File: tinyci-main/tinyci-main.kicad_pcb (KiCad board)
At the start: 2 copper layers, 110 x 82.5 mm, 56 parts, among them J1 Jack-DC, J2 Jack-DC, J3 Jack-DC, J4 Conn_01x13_Male, J5 Conn_01x13_Male, J6 Jack-DC, J7 Jack-DC, J8 Conn_01x04_Male, J9 Conn_01x04_Male, K1 SANYOU_SRD_Form_C, K2 SANYOU_SRD_Form_C, K3 SANYOU_SRD_Form_C, K4 SANYOU_SRD_Form_C, Q1 BC337, Q2 BC337, Q3 BC337, Q4 BC337, U1 AMS1117-3.3

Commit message: Version v0.5
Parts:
- removed G***: LOGO, tinyci:just-ci-it
- J8, J9: value Conn_01x04_Male -> Conn_01x06_Male
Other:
- board text added: "TinyCI v0.5"
- board text added: "TinyCI v0.5 http://github.com/superna9999/tinyci"
- board text removed: "TinyCI v0.4"
- board text removed: "TinyCI v0.4 http://github.com/superna9999/tinyci"

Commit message: fixup! Version v0.5
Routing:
- net VDC: track 136.6 -> 143.7 mm
- net /485_EN: track 55.4 -> 52.2 mm
- net /CFG: track 63.3 -> 60.2 mm
- net /IO17: track 40.7 -> 39.4 mm
- net /IO12: track 45.6 -> 44.5 mm
- net /IO5: track 48.1 -> 47.0 mm
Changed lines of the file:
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@@
     (thickness 1.6)
     (drawings 39)
-    (tracks 267)
+    (tracks 268)
     (zones 0)
     (modules 55)
@@
   (segment (start 153 101.6) (end 153 86.6) (width 2.5) (layer F.Cu) (net 2))
   (segment (start 112.25 118.4) (end 111.95 118.7) (width 2) (layer F.Cu) (net 2))
-  (segment (start 153 125) (end 153 114) (width 2.5) (layer F.Cu) (net 2))
   (segment (start 152.25 125.75) (end 153 125) (width 2.5) (layer F.Cu) (net 2))
   (segment (start 127.75 125.75) (end 152.25 125.75) (width 2.5) (layer F.Cu) (net 2))
@@
   (segment (start 107.7625 109.9) (end 105.3 109.9) (width 2.5) (layer F.Cu) (net 2))
   (segment (start 111.8625 114) (end 107.7625 109.9) (width 2.5) (layer F.Cu) (net 2))
+  (segment (start 151.25 114) (end 146.6 114) (width 2.5) (layer F.Cu) (net 2))
+  (segment (start 153 115.75) (end 151.25 114) (width 2.5) (layer F.Cu) (net 2))
+  (segment (start 153 125) (end 153 115.75) (width 2.5) (layer F.Cu) (net 2))
+  (segment (start 153 115.75) (end 153 114) (width 2.5) (layer F.Cu) (net 2))
   (segment (start 142.9 65.8) (end 148.55 71.45) (width 1) (layer F.Cu) (net 3))
   (segment (start 137.4 65.8) (end 142.9 65.8) (width 1) (layer F.Cu) (net 3))
@@
   (segment (start 143.1 114.6) (end 148.55 120.05) (width 1) (layer F.Cu) (net 6))
   (segment (start 137.2 114.6) (end 143.1 114.6) (width 1) (layer F.Cu) (net 6))
-  (segment (start 123.75 66.97) (end 118.75 61.97) (width 0.25) (layer B.Cu) (net 7))
-  (segment (start 118.75 61.97) (end 118.75 49.25) (width 0.25) (layer B.Cu) (net 7))
-  (segment (start 118.75 49.25) (end 118.75 49.25) (width 0.25) (layer B.Cu) (net 7))
-  (via (at 118.75 49.25) (size 0.8) (drill 0.4) (layers F.Cu B.Cu) (net 7))
-  (segment (start 134.34 49.25) (end 118.75 49.25) (width 0.25) (layer F.Cu) (net 7))
-  (segment (start 138.09 53) (end 134.34 49.25) (width 0.25) (layer F.Cu) (net 7))
+  (segment (start 118.75 50.75) (end 118.75 50.5) (width 0.25) (layer B.Cu) (net 7))
+  (via (at 118.75 50.75) (size 0.8) (drill 0.4) (layers F.Cu B.Cu) (net 7))
+  (segment (start 135.84 50.75) (end 118.75 50.75) (width 0.25) (layer F.Cu) (net 7))
+  (segment (start 138.09 53) (end 135.84 50.75) (width 0.25) (layer F.Cu) (net 7))
+  (segment (start 122.78 66) (end 123.75 66.97) (width 0.25) (layer B.Cu) (net 7))
+  (segment (start 121.75 66) (end 122.78 66) (width 0.25) (layer B.Cu) (net 7))
+  (segment (start 118.75 63) (end 121.75 66) (width 0.25) (layer B.Cu) (net 7))
+  (segment (start 118.75 50.75) (end 118.75 63) (width 0.25) (layer B.Cu) (net 7))
   (segment (start 123.75 69.51) (end 117.5 63.26) (width 0.25) (layer B.Cu) (net 8))
-  (segment (start 117.5 63.26) (end 117.5 49.25) (width 0.25) (layer B.Cu) (net 8))
-  (segment (start 117.5 49.25) (end 117.5 49.25) (width 0.25) (layer B.Cu) (net 8))
-  (via (at 117.5 49.25) (size 0.8) (drill 0.4) (layers F.Cu B.Cu) (net 8))
-  (segment (start 117.899999 48.850001) (end 117.5 49.25) (width 0.25) (layer F.Cu) (net 8))
-  (segment (start 118.225001 48.524999) (end 117.899999 48.850001) (width 0.25) (layer F.Cu) (net 8))
-  (segment (start 136.154999 48.524999) (end 118.225001 48.524999) (width 0.25) (layer F.Cu) (net 8))
-  (segment (start 140.63 53) (end 136.154999 48.524999) (width 0.25) (layer F.Cu) (net 8))
+  (segment (start 117.5 63.26) (end 117.5 50.75) (width 0.25) (layer B.Cu) (net 8))
+  (via (at 117.5 50.75) (size 0.8) (drill 0.4) (layers F.Cu B.Cu) (net 8))
+  (segment (start 117.899999 50.350001) (end 117.5 50.75) (width 0.25) (layer F.Cu) (net 8))
+  (segment (start 140.63 53) (end 137.13 49.5) (width 0.25) (layer F.Cu) (net 8))
+  (segment (start 118.75 49.5) (end 117.5 50.75) (width 0.25) (layer F.Cu) (net 8))
+  (segment (start 137.13 49.5) (end 118.75 49.5) (width 0.25) (layer F.Cu) (net 8))
   (segment (start 92.154999 75.954999) (end 91 74.8) (width 0.25) (layer B.Cu) (net 9))
   (segment (start 113.854999 75.954999) (end 92.154999 75.954999) (width 0.25) (layer B.Cu) (net 9))
@@
   (segment (start 160.8 108) (end 160.8 110.6) (width 2) (layer F.Cu) (net 24))
   (segment (start 123.75 72.05) (end 116.25 64.55) (width 0.25) (layer B.Cu) (net 27))
-  (segment (start 116.25 64.55) (end 116.25 49.25) (width 0.25) (layer B.Cu) (net 27))
-  (segment (start 116.25 49.25) (end 116.25 49.25) (width 0.25) (layer B.Cu) (net 27))
-  (via (at 116.25 49.25) (size 0.8) (drill 0.4) (layers F.Cu B.Cu) (net 27))
-  (segment (start 141.994999 54.175001) (end 134.175001 54.175001) (width 0.25) (layer F.Cu) (net 27))
+  (segment (start 116.25 64.55) (end 116.25 51.5) (width 0.25) (layer B.Cu) (net 27))
+  (via (at 116.25 51.5) (size 0.8) (drill 0.4) (layers F.Cu B.Cu) (net 27))
+  (segment (start 128.13641 51.5) (end 116.25 51.5) (width 0.25) (layer F.Cu) (net 27))
+  (segment (start 130.811411 54.175001) (end 128.13641 51.5) (width 0.25) (layer F.Cu) (net 27))
+  (segment (start 141.994999 54.175001) (end 130.811411 54.175001) (width 0.25) (layer F.Cu) (net 27))
   (segment (start 143.17 53) (end 141.994999 54.175001) (width 0.25) (layer F.Cu) (net 27))
-  (segment (start 116.649999 49.649999) (end 116.25 49.25) (width 0.25) (layer F.Cu) (net 27))
-  (segment (start 116.975001 49.975001) (end 116.649999 49.649999) (width 0.25) (layer F.Cu) (net 27))
-  (segment (start 129.975001 49.975001) (end 116.975001 49.975001) (width 0.25) (layer F.Cu) (net 27))
-  (segment (start 134.175001 54.175001) (end 129.975001 49.975001) (width 0.25) (layer F.Cu) (net 27))
   (segment (start 122.547919 74.59) (end 115 67.042081) (width 0.25) (layer B.Cu) (net 28))
+  (segment (start 115 67.042081) (end 115 52.25) (width 0.25) (layer B.Cu) (net 28))
   (segment (start 123.75 74.59) (end 122.547919 74.59) (width 0.25) (layer B.Cu) (net 28))
-  (segment (start 115 67.042081) (end 115 49.25) (width 0.25) (layer B.Cu) (net 28))
-  (segment (start 115 49.25) (end 115 49.25) (width 0.25) (layer B.Cu) (net 28))
-  (via (at 115 49.25) (size 0.8) (drill 0.4) (layers F.Cu B.Cu) (net 28))
-  (segment (start 144.084989 54.625011) (end 133.125011 54.625011) (width 0.25) (layer F.Cu) (net 28))
-  (segment (start 145.71 53) (end 144.084989 54.625011) (width 0.25) (layer F.Cu) (net 28))
-  (segment (start 116.175011 50.425011) (end 115.399999 49.649999) (width 0.25) (layer F.Cu) (net 28))
-  (segment (start 128.925011 50.425011) (end 116.175011 50.425011) (width 0.25) (layer F.Cu) (net 28))
-  (segment (start 115.399999 49.649999) (end 115 49.25) (width 0.25) (layer F.Cu) (net 28))
-  (segment (start 133.125011 54.625011) (end 128.925011 50.425011) (width 0.25) (layer F.Cu) (net 28))
+  (via (at 115 52.25) (size 0.8) (drill 0.4) (layers F.Cu B.Cu) (net 28))
+  (segment (start 129.125011 54.625011) (end 126.75 52.25) (width 0.25) (layer F.Cu) (net 28))
+  (segment (start 145.28707 54.625011) (end 129.125011 54.625011) (width 0.25) (layer F.Cu) (net 28))
+  (segment (start 126.75 52.25) (end 116.25 52.25) (width 0.25) (layer F.Cu) (net 28))
+  (segment (start 145.71 54.202081) (end 145.28707 54.625011) (width 0.25) (layer F.Cu) (net 28))
+  (segment (start 145.71 53) (end 145.71 54.202081) (width 0.25) (layer F.Cu) (net 28))
+  (segment (start 116.25 52.25) (end 115 52.25) (width 0.25) (layer F.Cu) (net 28))
+  (segment (start 116.75 52.25) (end 116.25 52.25) (width 0.25) (layer F.Cu) (net 28))
   (segment (start 130 67.25) (end 130 65.6) (width 0.25) (layer F.Cu) (net 30))
   (segment (start 99.099999 57.659999) (end 98.25 56.81) (width 0.25) (layer F.Cu) (net 30))
@@
   (segment (start 130.1 82.75) (end 130 82.65) (width 0.25) (layer F.Cu) (net 31))
   (segment (start 130.1 88.25) (end 130.1 82.75) (width 0.25) (layer F.Cu) (net 31))
-  (segment (start 135.55 53) (end 131.074999 48.524999) (width 0.25) (layer B.Cu) (net 33))
-  (segment (start 114.475001 48.524999) (end 113.25 49.75) (width 0.25) (layer B.Cu) (net 33))
-  (segment (start 131.074999 48.524999) (end 114.475001 48.524999) (width 0.25) (layer B.Cu) (net 33))
-  (segment (start 113.25 49.75) (end 98.25 64.43) (width 0.25) (layer B.Cu) (net 33))
+  (segment (start 99.099999 63.580001) (end 98.25 64.43) (width 0.25) (layer B.Cu) (net 33))
+  (segment (start 112.655001 50.024999) (end 99.099999 63.580001) (width 0.25) (layer B.Cu) (net 33))
+  (segment (start 132.574999 50.024999) (end 112.655001 50.024999) (width 0.25) (layer B.Cu) (net 33))
+  (segment (start 135.55 53) (end 132.574999 50.024999) (width 0.25) (layer B.Cu) (net 33))
   (segment (start 97.67 80.25) (end 98.25 79.67) (width 0.25) (layer F.Cu) (net 36))
   (segment (start 98.04 79.88) (end 98.25 79.67) (width 0.25) (layer F.Cu) (net 36))

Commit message: fixup! fixup! Version v0.5
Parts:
- added G***: LOGO, TinyCI:just-ci-it, B.Cu at (167.2, 84.8)

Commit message: Add LICENCE to TinyCI-main
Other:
- board text added: "TinyCI v0.5 http://github.com/superna9999/tinyci CERN OPEN HARDWARE LICENCE v1.1"
- board text removed: "TinyCI v0.5 http://github.com/superna9999/tinyci"
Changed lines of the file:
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@@
     )
   )
-  (gr_text "TinyCI v0.5\nhttp://github.com/superna9999/tinyci" (at 104.5 87.75 90) (layer B.SilkS)
+  (gr_text "TinyCI v0.5\nhttp://github.com/superna9999/tinyci\n\nCERN OPEN HARDWARE LICENCE v1.1" (at 109.25 85 90) (layer B.SilkS)
     (effects (font (size 3 2.5) (thickness 0.5)) (justify mirror))
   )

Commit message: Ordered Version !
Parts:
- added USB0: USB_A_Stewart_SS-52100-001_Horizontal, Connector_USB:USB_A_Stewart_SS-52100-001_Horizontal, F.Cu at (186.0, 69.0)
- added USB1: USB_A_Stewart_SS-52100-001_Horizontal, Connector_USB:USB_A_Stewart_SS-52100-001_Horizontal, F.Cu at (186.0, 87.0)
- added USB2: USB_A_Stewart_SS-52100-001_Horizontal, Connector_USB:USB_A_Stewart_SS-52100-001_Horizontal, F.Cu at (186.0, 105.0)
- added USB3: USB_A_Stewart_SS-52100-001_Horizontal, Connector_USB:USB_A_Stewart_SS-52100-001_Horizontal, F.Cu at (186.0, 123.0)
- moved J7 4.70 mm to (189.2, 121.8)
- moved J2 3.40 mm to (189.2, 68.0)
- moved J6 3.01 mm to (189.2, 104.0)
- moved J3 2.00 mm to (189.2, 86.0)
- moved J5 1.90 mm to (100.1, 85.2)
- moved J4 0.83 mm to (123.0, 85.2)
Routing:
- net GND: track 57.4 -> 75.6 mm
- net Net-(C6-Pad1): track 27.1 -> 32.4 mm
- net /IO4: track 47.9 -> 51.7 mm
- net Net-(C2-Pad1): track 26.0 -> 29.1 mm
- net Net-(C4-Pad1): track 26.1 -> 28.8 mm
- net Net-(C5-Pad1): track 26.0 -> 28.6 mm
- net /IO2: track 41.5 -> 39.5 mm
- net /IO3: track 7.39 -> 9.20 mm
- net /IO12: track 44.5 -> 42.8 mm
- net /EN: track 36.9 -> 38.2 mm
- net /IO15: track 65.1 -> 63.9 mm
- net /IO1: track 8.04 -> 9.20 mm
- net /IO0: track 8.16 -> 9.20 mm
- net /IO14: track 51.9 -> 51.3 mm
- net /CFG: track 60.2 -> 59.7 mm
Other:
- board text added: "DC 5V"
- board text added: "JLCJLCJLCJLC"

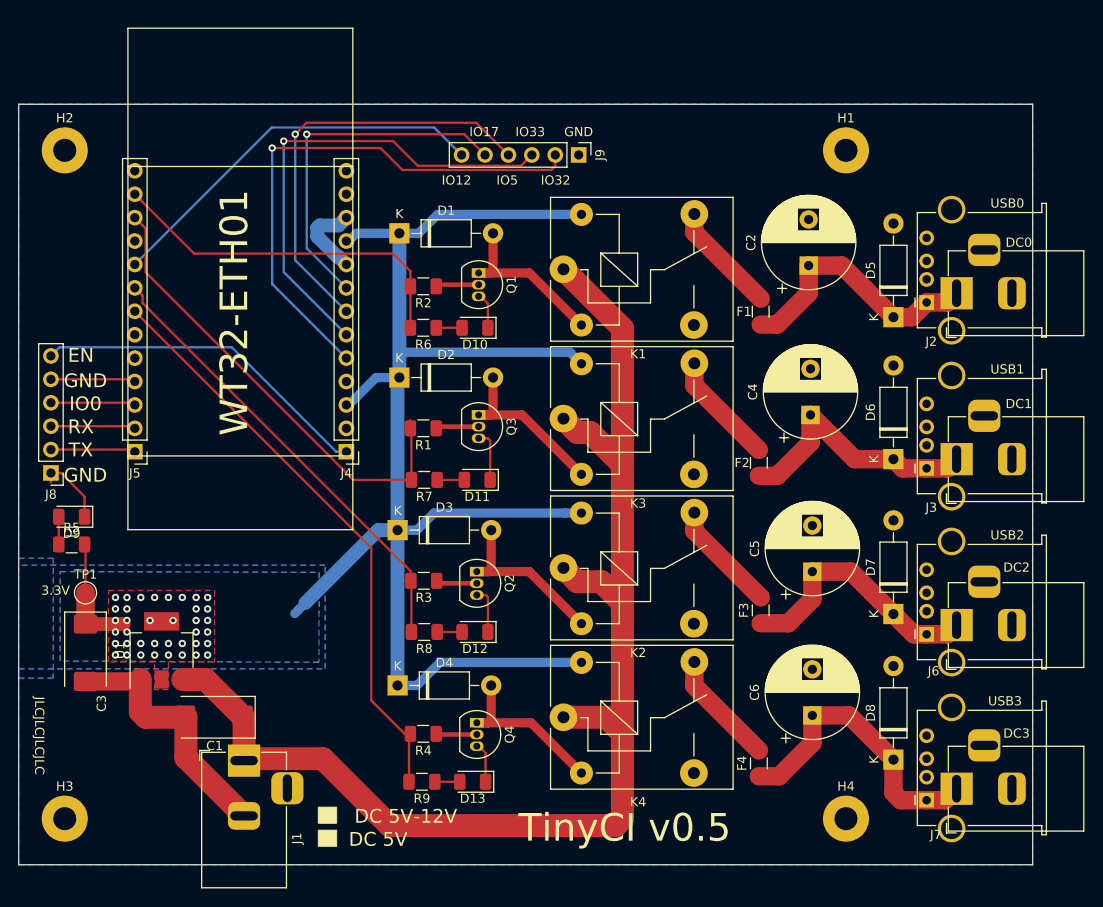
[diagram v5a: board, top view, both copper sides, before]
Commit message: TinyCI 0.6
- Fixed bad relay output (outputs must be disabled by default, activating the relay will send power to outputs)
- grow mounting hole to 3.2mm to target M3 screws
- removed "5v-12v" text, this board will be 5V only, LDO heats too much at 12V
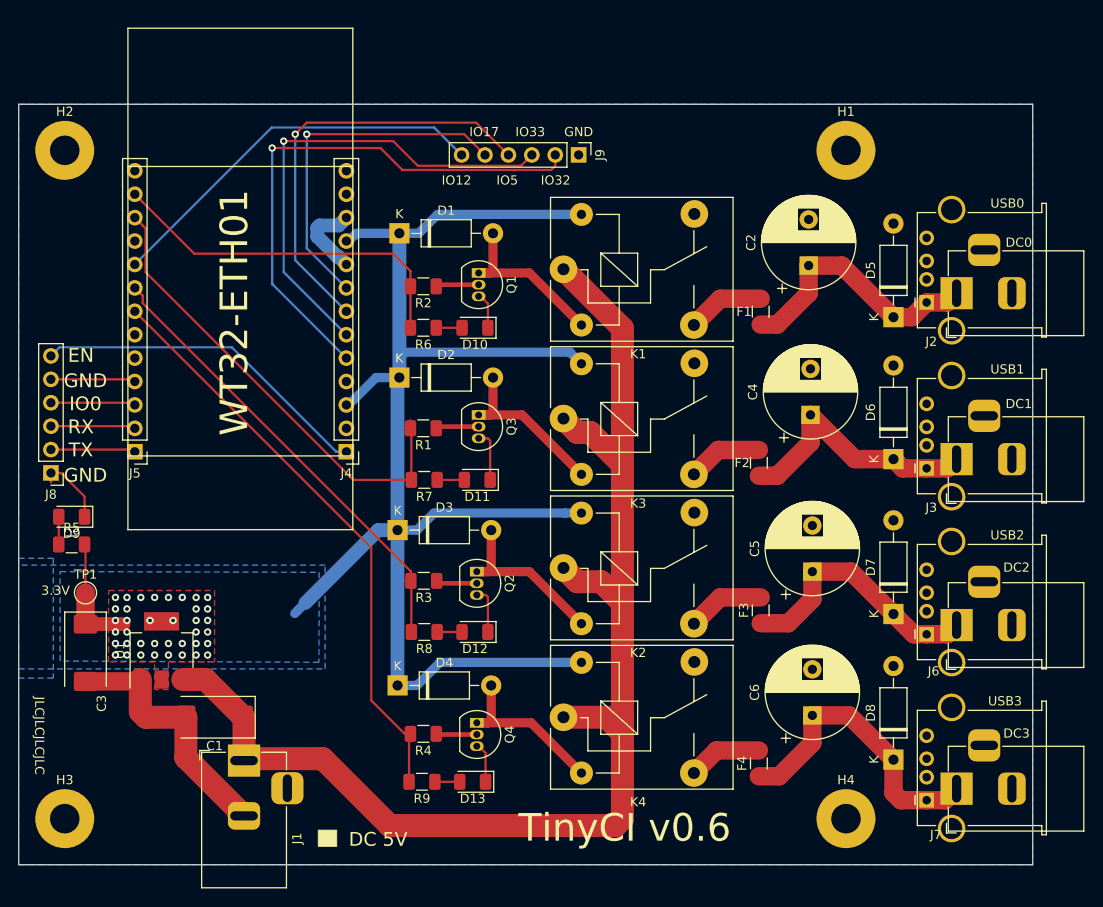
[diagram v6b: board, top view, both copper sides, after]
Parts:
- H1, H2, H3, H4: footprint MountingHole:MountingHole_2.5mm_Pad -> MountingHole:MountingHole_3.2mm_M3_Pad
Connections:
- K1 pad 3: Net-(K1-Pad3) -> /NO_1
- K1 pad 4: /NO_1 -> Net-(K1-Pad4)
- K2 pad 3: Net-(K2-Pad3) -> /NO_3
- K2 pad 4: /NO_3 -> Net-(K2-Pad4)
- K3 pad 3: Net-(K3-Pad3) -> /NO_2
- K3 pad 4: /NO_2 -> Net-(K3-Pad4)
- K4 pad 3: Net-(K4-Pad3) -> /NO_4
- K4 pad 4: /NO_4 -> Net-(K4-Pad4)
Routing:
- net /NO_4: track 12.5 -> 8.06 mm
- net /NO_2: track 12.3 -> 8.15 mm
- net /NO_3: track 12.2 -> 8.43 mm
- net /NO_1: track 12.2 -> 8.43 mm
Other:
- board text added: "TinyCI v0.6"
- board text added: "TinyCI v0.6 http://github.com/superna9999/tinyci CERN OPEN HARDWARE LICENCE v1.1"
- board text removed: "DC 5V-12V"
- board text removed: "TinyCI v0.5"
- board text removed: "TinyCI v0.5 http://github.com/superna9999/tinyci CERN OPEN HARDWARE LICENCE v1.1"

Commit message: TinyCI Main v0.7
Remove post-relay protections, and move 1000uF caps before relay.

Add proper OSHW & Made with KiCad logo

Signed-off-by: Neil Armstrong <narmstrong@baylibre.com>
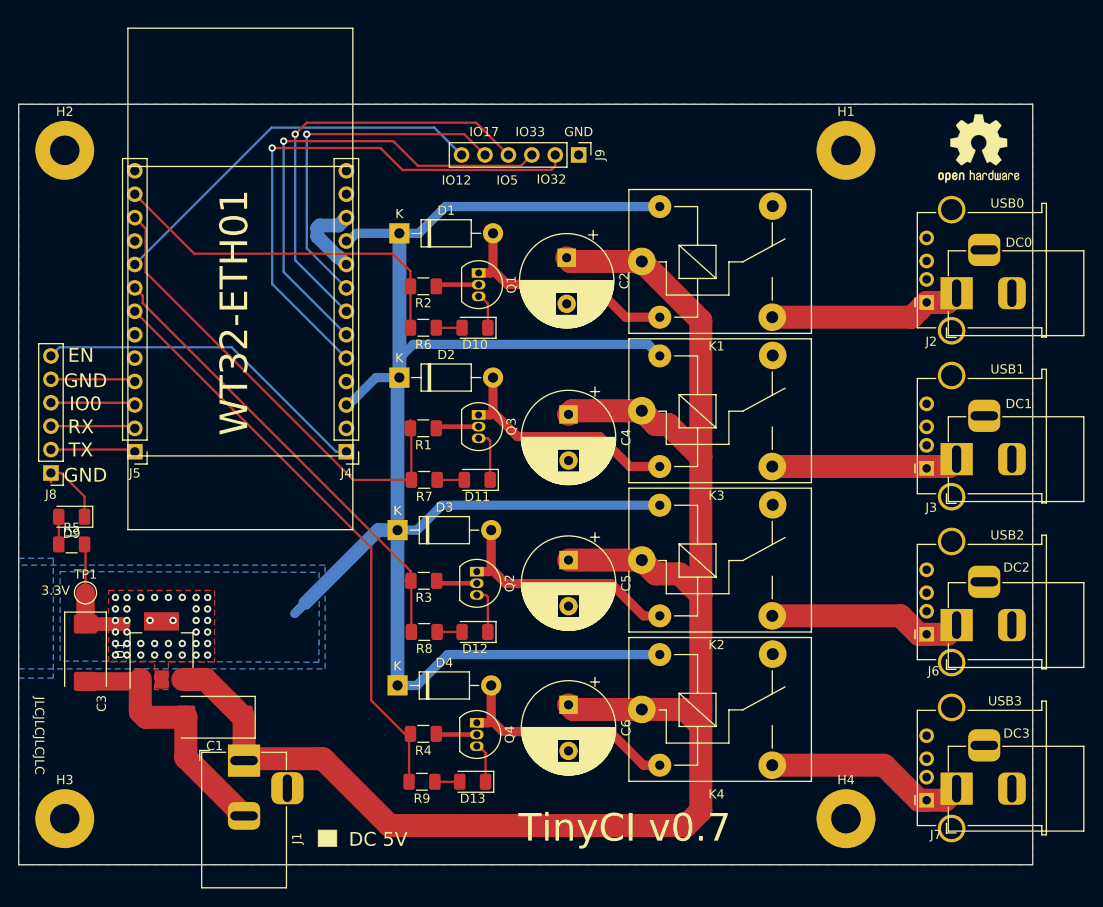
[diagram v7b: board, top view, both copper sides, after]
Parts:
- removed D5, D6, D7, D8: 1N4001, Diode_THT:D_DO-41_SOD81_P10.16mm_Horizontal
- removed F1, F2, F3, F4: Polyfuse, Fuse:Fuse_1206_3216Metric
- added REF**: OSHW-Logo2_9.8x8mm_SilkScreen, Symbol:OSHW-Logo2_9.8x8mm_SilkScreen, F.Cu at (191.7, 52.3)
- added REF**: KiCad-Logo2_5mm_SilkScreen, Symbol:KiCad-Logo2_5mm_SilkScreen, B.Cu at (92.2, 64.5)
- moved C5 26.5 mm to (147.2, 97.0), turned to 270 degrees
- moved C6 26.5 mm to (147.2, 112.7), turned to 270 degrees
- moved C2 26.3 mm to (146.9, 64.2), turned to 270 degrees
- moved C4 26.3 mm to (147.2, 81.2), turned to 270 degrees
- moved K1 8.54 mm to (155.1, 64.5)
- moved K2 8.54 mm to (155.1, 97.0)
- moved K3 8.54 mm to (155.1, 80.8)
- moved K4 8.54 mm to (155.1, 113.2)
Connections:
- C2 pad 1: Net-(C2-Pad1) -> VDC
- C4 pad 1: Net-(C4-Pad1) -> VDC
- C5 pad 1: Net-(C5-Pad1) -> VDC
- C6 pad 1: Net-(C6-Pad1) -> VDC
- J2 pad 1: Net-(C2-Pad1) -> /NO_1
- J3 pad 1: Net-(C4-Pad1) -> /NO_2
- J6 pad 1: Net-(C5-Pad1) -> /NO_3
- J7 pad 1: Net-(C6-Pad1) -> /NO_4
- USB0 pad 1: Net-(C2-Pad1) -> /NO_1
- USB1 pad 1: Net-(C4-Pad1) -> /NO_2
- USB2 pad 1: Net-(C5-Pad1) -> /NO_3
- USB3 pad 1: Net-(C6-Pad1) -> /NO_4
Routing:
- net VDC: track 143.7 -> 185.1 mm
- net +3V3: track 174.3 -> 209.7 mm
- net Net-(C6-Pad1): track 32.4 -> 0.00 mm
- net Net-(C2-Pad1): track 29.1 -> 0.00 mm
- net Net-(C4-Pad1): track 28.8 -> 0.00 mm
- net Net-(C5-Pad1): track 28.6 -> 0.00 mm
- net /NO_4: track 8.06 -> 22.1 mm
- net /NO_3: track 8.43 -> 21.2 mm
- net /NO_1: track 8.43 -> 21.1 mm
- net /NO_2: track 8.15 -> 20.3 mm
- net /COIL_1_4: track 19.0 -> 25.8 mm
- net /COIL_1_3: track 19.6 -> 26.3 mm
- net /COIL_1_2: track 19.3 -> 26.0 mm
- net /COIL_1_1: track 19.2 -> 25.9 mm
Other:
- board text added: "TinyCI v0.7"
- board text added: "TinyCI v0.7 http://github.com/superna9999/tinyci CERN OPEN HARDWARE LICENCE v1.1"
- board text removed: "TinyCI v0.6"
- board text removed: "TinyCI v0.6 http://github.com/superna9999/tinyci CERN OPEN HARDWARE LICENCE v1.1"

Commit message: tinyci-main: Converted PCB to KiCad 6.
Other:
- net class Default removed
